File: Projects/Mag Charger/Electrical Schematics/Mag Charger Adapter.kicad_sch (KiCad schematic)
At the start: 4 parts, among them J1 Conn_01x08, J3 DX07S016JA3R1500

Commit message: Updated diode models
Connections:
- net USB_DN: now also D2.1 (K); no longer D2.2 (K)
- net USB_DP: now also D2.2 (K); no longer D2.1 (K)
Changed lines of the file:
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@@
-		)
-	)
-	(label "USB_DP"
-		(at 68.58 67.31 180)
-		(effects
-			(font
-				(size 1.27 1.27)
-			)
-			(justify right bottom)
-		)
-	)
-	(label "USB_DN"
-		(at 73.66 64.77 180)
-		(effects
-			(font
-				(size 1.27 1.27)
-			)
-			(justify right bottom)
 		)
 	)
@@
 		)
 	)
+	(label "USB_DN"
+		(at 68.58 67.31 180)
+		(effects
+			(font
+				(size 1.27 1.27)
+			)
+			(justify right bottom)
+		)
+	)
+	(label "USB_DP"
+		(at 73.66 64.77 180)
+		(effects
+			(font
+				(size 1.27 1.27)
+			)
+			(justify right bottom)
+		)
+	)

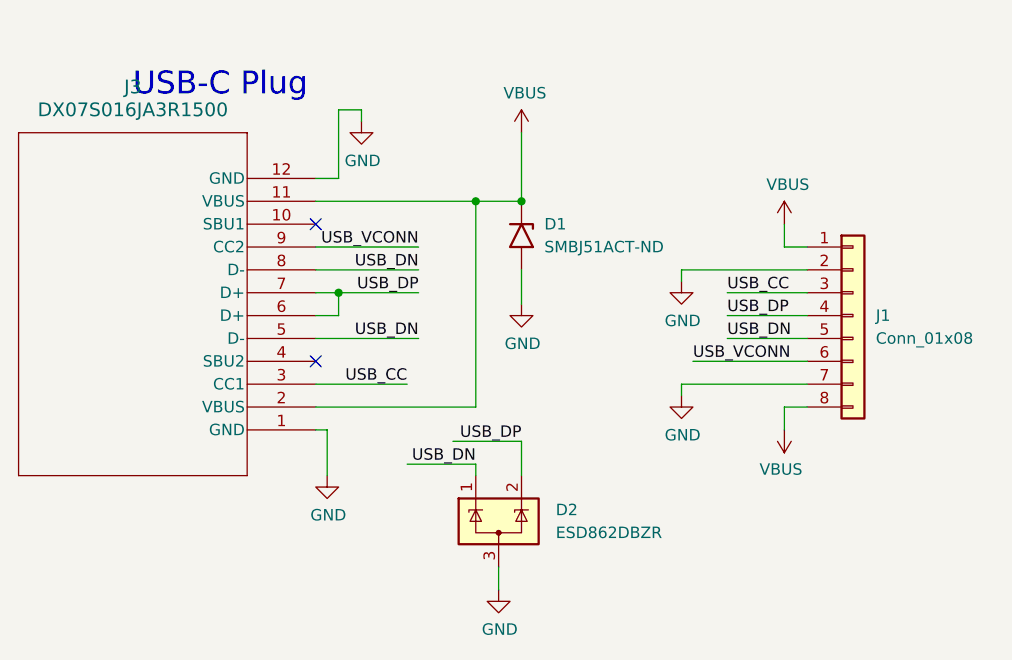
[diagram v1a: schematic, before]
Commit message: Updated mag charger design
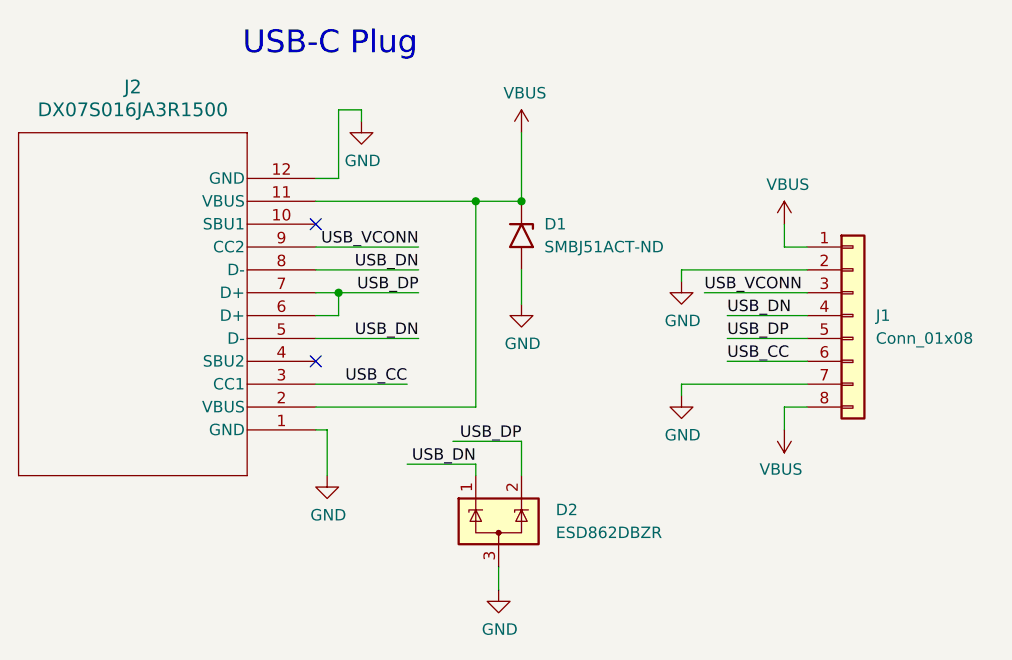
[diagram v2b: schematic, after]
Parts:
- D1: footprint D_SMB_Handsoldering -> D_SMB
- renumbered J3 to J2
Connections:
- net USB_CC: now also J1.6 (Pin_6); no longer J1.3 (Pin_3)
- net USB_DN: now also J1.4 (Pin_4); no longer J1.5 (Pin_5)
- net USB_DP: now also J1.5 (Pin_5); no longer J1.4 (Pin_4)
- net USB_VCONN: now also J1.3 (Pin_3); no longer J1.6 (Pin_6)
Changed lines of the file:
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@@
 	(text "USB-C Plug"
 		(exclude_from_sim no)
-		(at 30.48 26.67 0)
+		(at 42.672 22.098 0)
 		(effects
 			(font
@@
 	(wire
 		(pts
+			(xy 96.52 55.88) (xy 105.41 55.88)
+		)
+		(stroke
+			(width 0)
+			(type default)
+		)
+	)
+	(wire
+		(pts
 			(xy 50.8 50.8) (xy 53.34 50.8)
 		)
@@
 	(wire
 		(pts
-			(xy 96.52 48.26) (xy 105.41 48.26)
-		)
-		(stroke
-			(width 0)
-			(type default)
-		)
-	)
-	(wire
-		(pts
 			(xy 50.8 58.42) (xy 60.96 58.42)
 		)
@@
 	(wire
 		(pts
-			(xy 92.71 55.88) (xy 105.41 55.88)
-		)
-		(stroke
-			(width 0)
-			(type default)
-		)
-	)
-	(wire
-		(pts
 			(xy 50.8 43.18) (xy 62.23 43.18)
 		)
@@
 	(wire
 		(pts
+			(xy 93.98 48.26) (xy 105.41 48.26)
+		)
+		(stroke
+			(width 0)
+			(type default)
+		)
+	)
+	(wire
+		(pts
 			(xy 102.87 43.18) (xy 102.87 40.64)
 		)
@@
 			(width 0)
 			(type default)
-		)
-	)
-	(label "USB_DN"
-		(at 96.52 53.34 0)
-		(effects
-			(font
-				(size 1.27 1.27)
-			)
-			(justify left bottom)
 		)
 	)
@@
 		)
 	)
+	(label "USB_CC"
+		(at 96.52 55.88 0)
+		(effects
+			(font
+				(size 1.27 1.27)
+			)
+			(justify left bottom)
+		)
+	)
 	(label "USB_DN"
 		(at 62.23 53.34 180)
@@
 		)
 	)
-	(label "USB_CC"
-		(at 96.52 48.26 0)
+	(label "USB_DN"
+		(at 96.52 50.8 0)
 		(effects
 			(font
@@
 		)
 	)
-	(label "USB_DP"
-		(at 96.52 50.8 0)
+	(label "USB_VCONN"
+		(at 93.98 48.26 0)
 		(effects
 			(font
@@
 		)
 	)
-	(label "USB_VCONN"
-		(at 92.71 55.88 0)
+	(label "USB_DP"
+		(at 96.52 53.34 0)
 		(effects
 			(font
@@
 			)
 		)
-		(property "Footprint" "D_SMB_Handsoldering"
+		(property "Footprint" "D_SMB"
 			(at 68.58 41.91 0)
 			(effects
@@
 		(dnp no)
 		(fields_autoplaced yes)
-		(property "Reference" "J3"
+		(property "Reference" "J2"
 			(at 30.48 25.4 0)
 			(effects
@@
 			(project ""
 				(path "/7d4a0788-2acd-4c20-8b55-4c42f19a8596"
-					(reference "J3")
+					(reference "J2")
 					(unit 1)
 				)
